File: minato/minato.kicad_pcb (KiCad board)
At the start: 2 copper layers, 400.1 x 144.5 mm, 220 parts, among them U2 STM32F103C8Tx

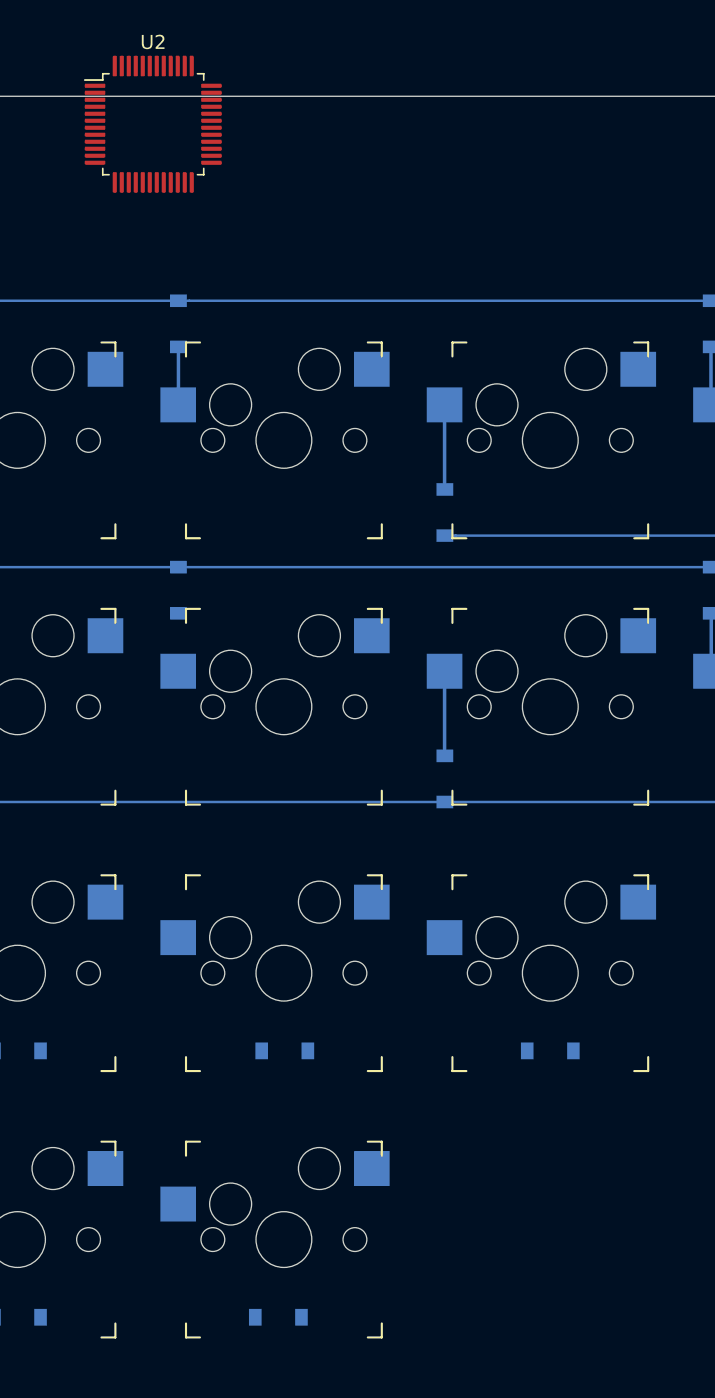
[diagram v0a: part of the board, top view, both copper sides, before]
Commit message: :sparkles: Add crystal + HW reset
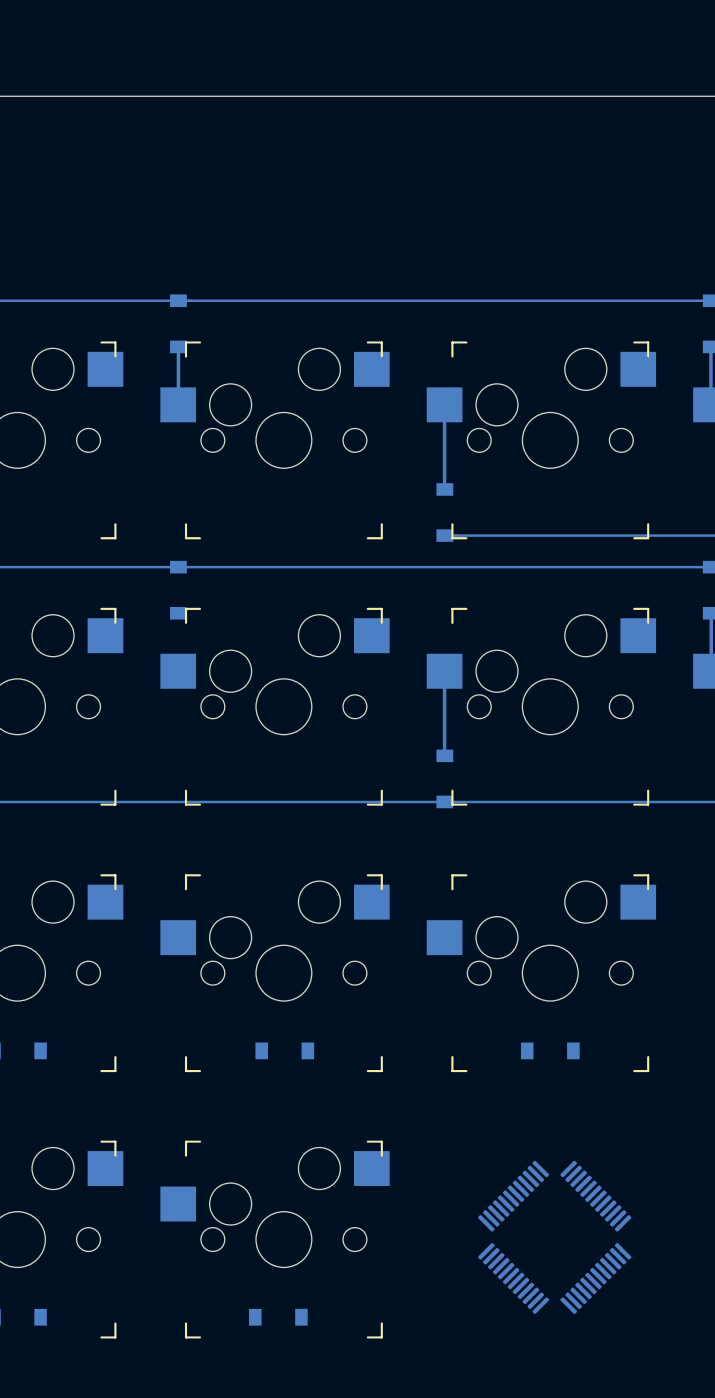
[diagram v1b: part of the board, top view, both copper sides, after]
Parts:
- U2: moved to B.Cu
- moved U2 84.6 mm to (94.0, 99.1), turned to 45 degrees

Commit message: :construction: WIP
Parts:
- removed the HOLE_M3 at (414.7, 20.2)
- removed the HOLE_M3 at (414.7, 159.1)
- removed the HOLE_M3 at (20.2, 159.1)
- added C1: 4.7nF, Capacitor_SMD:C_0805_2012Metric, F.Cu at (138.9, -7.29)
- added C10: 100nF, Capacitor_SMD:C_0805_2012Metric, F.Cu at (85.5, 95.2)
- added C11: 10nF, Capacitor_SMD:C_0805_2012Metric, F.Cu at (150.3, -22.3)
- added C12: 1uF, Capacitor_SMD:C_0805_2012Metric, F.Cu at (141.9, -12.3)
- added C2: 10uF, Capacitor_SMD:C_0805_2012Metric, F.Cu at (143.9, -27.4)
- added C3: 4.7nF, Capacitor_SMD:C_0805_2012Metric, F.Cu at (136.7, -23.8)
- added C6: 100nF, Capacitor_SMD:C_0805_2012Metric, F.Cu at (135.1, -16.1)
- added C7: 100nF, Capacitor_SMD:C_0805_2012Metric, F.Cu at (90.1, 107.2)
- added C8: 100nF, Capacitor_SMD:C_0805_2012Metric, F.Cu at (132.1, -7.15)
- added C9: 100nF, Capacitor_SMD:C_0805_2012Metric, F.Cu at (100.8, 104.4)
- added D106: 1N4148, keyboard_parts.pretty:D_SOD123W_hand, F.Cu at (137.1, -28.1)
- added D108: 1N4148, keyboard_parts.pretty:D_SOD123W_hand, F.Cu at (116.3, -18.3)
- added F1: Polyfuse_Small, Fuse:Fuse_1812_4532Metric, F.Cu at (125.2, -7.17)
- added HOLE_M3: VAL**, keyboard_parts.pretty:HOLE_M3, F.Cu at (414.3, 33.7)
- added HOLE_M3: VAL**, keyboard_parts.pretty:HOLE_M3, F.Cu at (414.3, 145.7)
- added HOLE_M3: VAL**, keyboard_parts.pretty:HOLE_M3, F.Cu at (20.6, 145.7)
- added J1: Conn_ARM_JTAG_SWD_10, Connector_IDC:IDC-Header_2x05_P2.54mm_Vertical, B.Cu at (89.3, 138.5)
- added J2: USB_C_Receptacle_USB2.0, Connector_USB:USB_C_Receptacle_GCT_USB4085, B.Cu at (46.8, 36.5)
- added Q1: DTC123J, Package_TO_SOT_SMD:SOT-23, F.Cu at (147.6, -17.6)
- added R1: 10k, keyboard_parts.pretty:R_2012, F.Cu at (151.9, -18.1)
- added R2: 1M, keyboard_parts.pretty:R_2012, F.Cu at (144.4, -8.06)
- added R3: 5.1k, keyboard_parts.pretty:R_2012, F.Cu at (151.9, -14.6)
- added R4: 5.1k, keyboard_parts.pretty:R_2012, F.Cu at (148.6, -9.00)
- added SW1: SW_Push, keyboard_parts.pretty:SW_ALPS_SKRP, F.Cu at (104.8, 99.2)
- added U1: MCP1700-3302E_SOT23, Package_TO_SOT_SMD:SOT-23, F.Cu at (147.6, -13.0)
- added Y1: 16MHz, local.pretty:OSC_CSTCE16M0V53-R0, F.Cu at (84.5, 102.8)
- D1, D10, D100, D101, D102, D103, D104, D105, D11, D12, D13, D14, D15, D16, D17, D18, D19, D2, D20, D21, D22, D23, D24, D25, D26, D27, D28, D29, D3, D30, D31, D32, D33, D34, D35, D36, D37, D38, D39, D4, D40, D41, D42, D43, D44, D45, D46, D47, D48, D49, D5, D50, D51, D52, D53, D54, D55, D56, D57, D58, D59, D6, D60, D61, D62, D63, D64, D65, D66, D67, D68, D69, D7, D70, D71, D72, D73, D74, D75, D76, D77, D78, D79, D8, D80, D81, D82, D83, D84, D85, D86, D87, D88, D89, D9, D90, D91, D92, D93, D94, D95, D96, D97, D98, D99: footprint Diode_SMD:D_SOD-123 -> keyboard_parts.pretty:D_SOD123W_hand
- U2: moved to F.Cu
- moved HOLE_M3 13.5 mm to (20.6, 33.7)
- moved U2 1.12 mm to (92.9, 99.2)
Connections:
- MX0:0 pad 1: Net-(MX0:0-Pad1) -> Col0
- U2 pad 1: Net-(U2-Pad1) -> VSS1
- U2 pad 23: Net-(U2-Pad23) -> VSS1
- U2 pad 24: Net-(U2-Pad24) -> 3.3V
- U2 pad 3: Net-(U2-Pad3) -> XTI
- U2 pad 35: Net-(U2-Pad35) -> VSS1
- U2 pad 36: Net-(U2-Pad36) -> 3.3V
- U2 pad 4: Net-(U2-Pad4) -> XTO
- U2 pad 44: Net-(U2-Pad44) -> BOOT0
- U2 pad 47: Net-(U2-Pad47) -> VSS1
- U2 pad 48: Net-(U2-Pad48) -> 3.3V
- U2 pad 8: Net-(U2-Pad8) -> VSS1
- U2 pad 9: Net-(U2-Pad9) -> 3.3V
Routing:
- net VSS1: track 0.00 -> 26.0 mm
- net 3.3V: track 0.00 -> 23.1 mm
- net XTO: track 0.00 -> 5.55 mm
- net XTI: track 0.00 -> 4.99 mm
- net Net-(D106-Pad2): track 0.00 -> 4.20 mm
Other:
- board size 400.1 x 144.5 mm -> 400.1 x 118.3 mm

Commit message: :construction: More PCB work
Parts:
- removed C10: 100nF, Capacitor_SMD:C_0805_2012Metric
- added Ce: 100nF, Capacitor_SMD:C_0805_2012Metric, F.Cu at (90.4, 91.9)
- moved C11 139.9 mm to (95.6, 106.4), turned to 180 degrees
- moved C12 129.6 mm to (95.6, 108.7), turned to 180 degrees
- moved D63 15.8 mm to (265.1, 47.6), turned to 180 degrees
- moved D64 15.8 mm to (265.1, 66.7), turned to 180 degrees
- moved D96 15.8 mm to (379.4, 47.6), turned to 180 degrees
- moved D1 15.8 mm to (36.5, 47.6), turned to 180 degrees
- moved D2 15.8 mm to (36.5, 66.7), turned to 180 degrees
- moved D22 15.8 mm to (112.7, 47.6), turned to 180 degrees
- moved D23 15.8 mm to (112.7, 66.7), turned to 180 degrees
- moved D31 15.8 mm to (150.8, 47.6), turned to 180 degrees
- moved D32 15.8 mm to (150.8, 66.7), turned to 180 degrees
- moved D43 15.8 mm to (188.9, 47.6), turned to 180 degrees
- moved D44 15.8 mm to (188.9, 66.7), turned to 180 degrees
- moved D12 15.8 mm to (74.6, 47.6), turned to 180 degrees
- moved D13 15.8 mm to (74.6, 66.7), turned to 180 degrees
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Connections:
- D1 pad 1: Row0 -> Net-(D1-Pad1)
- D1 pad 2: Net-(D1-Pad2) -> Col0
- D10 pad 1: Row7 -> Net-(D10-Pad1)
- D10 pad 2: Net-(D10-Pad2) -> Col0
- D100 pad 1: Row1 -> Net-(D100-Pad1)
- D100 pad 2: Net-(D100-Pad2) -> Col9
- D101 pad 1: Row2 -> Net-(D101-Pad1)
- D101 pad 2: Net-(D101-Pad2) -> Col9
- D102 pad 1: Row4 -> Net-(D102-Pad1)
- D102 pad 2: Net-(D102-Pad2) -> Col9
- D103 pad 1: Row6 -> Net-(D103-Pad1)
- D103 pad 2: Net-(D103-Pad2) -> Col8
- D104 pad 1: Row9 -> Net-(D104-Pad1)
- D104 pad 2: Net-(D104-Pad2) -> Col8
- D105 pad 1: Row11 -> Net-(D105-Pad1)
- D105 pad 2: Net-(D105-Pad2) -> Col5
- D11 pad 1: Row9 -> Net-(D11-Pad1)
- D11 pad 2: Net-(D11-Pad2) -> Col0
- D12 pad 1: Row0 -> Net-(D12-Pad1)
- D12 pad 2: Net-(D12-Pad2) -> Col1
- D13 pad 1: Row2 -> Net-(D13-Pad1)
- D13 pad 2: Net-(D13-Pad2) -> Col1
- D14 pad 1: Row4 -> Net-(D14-Pad1)
- D14 pad 2: Net-(D14-Pad2) -> Col1
- D15 pad 1: Row6 -> Net-(D15-Pad1)
- D15 pad 2: Net-(D15-Pad2) -> Col1
- D16 pad 1: Row8 -> Net-(D16-Pad1)
- D16 pad 2: Net-(D16-Pad2) -> Col1
- D17 pad 1: Row11 -> Net-(D17-Pad1)
- D17 pad 2: Net-(D17-Pad2) -> Col0
- D18 pad 1: Row1 -> Net-(D18-Pad1)
- D18 pad 2: Net-(D18-Pad2) -> Col1
- D19 pad 1: Row3 -> Net-(D19-Pad1)
- D19 pad 2: Net-(D19-Pad2) -> Col1
- D2 pad 1: Row2 -> Net-(D2-Pad1)
- D2 pad 2: Net-(D2-Pad2) -> Col0
- D20 pad 1: Row5 -> Net-(D20-Pad1)
- D20 pad 2: Net-(D20-Pad2) -> Col1
- D21 pad 1: Row9 -> Net-(D21-Pad1)
- D21 pad 2: Net-(D21-Pad2) -> Col1
- D22 pad 1: Row0 -> Net-(D22-Pad1)
- D22 pad 2: Net-(D22-Pad2) -> Col2
- D23 pad 1: Row2 -> Net-(D23-Pad1)
- D23 pad 2: Net-(D23-Pad2) -> Col2
- D24 pad 1: Row4 -> Net-(D24-Pad1)
- D24 pad 2: Net-(D24-Pad2) -> Col2
- D25 pad 1: Row7 -> Net-(D25-Pad1)
- D25 pad 2: Net-(D25-Pad2) -> Col1
- D26 pad 1: Row8 -> Net-(D26-Pad1)
- D26 pad 2: Net-(D26-Pad2) -> Col2
- D27 pad 1: Row10 -> Net-(D27-Pad1)
- D27 pad 2: Net-(D27-Pad2) -> Col1
- D28 pad 1: Row1 -> Net-(D28-Pad1)
- D28 pad 2: Net-(D28-Pad2) -> Col2
- D29 pad 1: Row3 -> Net-(D29-Pad1)
- D29 pad 2: Net-(D29-Pad2) -> Col2
- D3 pad 1: Row4 -> Net-(D3-Pad1)
- D3 pad 2: Net-(D3-Pad2) -> Col0
- D30 pad 1: Row11 -> Net-(D30-Pad1)
- D30 pad 2: Net-(D30-Pad2) -> Col1
- D31 pad 1: Row0 -> Net-(D31-Pad1)
- D31 pad 2: Net-(D31-Pad2) -> Col3
- D32 pad 1: Row2 -> Net-(D32-Pad1)
- D32 pad 2: Net-(D32-Pad2) -> Col3
- D33 pad 1: Row5 -> Net-(D33-Pad1)
- D33 pad 2: Net-(D33-Pad2) -> Col2
- D34 pad 1: Row6 -> Net-(D34-Pad1)
- D34 pad 2: Net-(D34-Pad2) -> Col2
- D35 pad 1: Row9 -> Net-(D35-Pad1)
- D35 pad 2: Net-(D35-Pad2) -> Col2
- D36 pad 1: Row10 -> Net-(D36-Pad1)
- D36 pad 2: Net-(D36-Pad2) -> Col2
- D37 pad 1: Row1 -> Net-(D37-Pad1)
- D37 pad 2: Net-(D37-Pad2) -> Col3
- D38 pad 1: Row3 -> Net-(D38-Pad1)
- D38 pad 2: Net-(D38-Pad2) -> Col3
- D39 pad 1: Row4 -> Net-(D39-Pad1)
- D39 pad 2: Net-(D39-Pad2) -> Col3
- D4 pad 1: Row6 -> Net-(D4-Pad1)
- D4 pad 2: Net-(D4-Pad2) -> Col0
- D40 pad 1: Row7 -> Net-(D40-Pad1)
- D40 pad 2: Net-(D40-Pad2) -> Col2
- D41 pad 1: Row8 -> Net-(D41-Pad1)
- D41 pad 2: Net-(D41-Pad2) -> Col3
- D42 pad 1: Row11 -> Net-(D42-Pad1)
- D42 pad 2: Net-(D42-Pad2) -> Col2
- D43 pad 1: Row0 -> Net-(D43-Pad1)
- D43 pad 2: Net-(D43-Pad2) -> Col4
- D44 pad 1: Row2 -> Net-(D44-Pad1)
- D44 pad 2: Net-(D44-Pad2) -> Col4
- D45 pad 1: Row5 -> Net-(D45-Pad1)
- D45 pad 2: Net-(D45-Pad2) -> Col3
- D46 pad 1: Row6 -> Net-(D46-Pad1)
- D46 pad 2: Net-(D46-Pad2) -> Col3
- D47 pad 1: Row9 -> Net-(D47-Pad1)
- D47 pad 2: Net-(D47-Pad2) -> Col3
- D48 pad 1: Row1 -> Net-(D48-Pad1)
- D48 pad 2: Net-(D48-Pad2) -> Col4
- D49 pad 1: Row3 -> Net-(D49-Pad1)
- D49 pad 2: Net-(D49-Pad2) -> Col4
- D5 pad 1: Row8 -> Net-(D5-Pad1)
- D5 pad 2: Net-(D5-Pad2) -> Col0
- D50 pad 1: Row4 -> Net-(D50-Pad1)
- D50 pad 2: Net-(D50-Pad2) -> Col4
- D51 pad 1: Row7 -> Net-(D51-Pad1)
- D51 pad 2: Net-(D51-Pad2) -> Col3
- D52 pad 1: Row8 -> Net-(D52-Pad1)
- D52 pad 2: Net-(D52-Pad2) -> Col4
- D53 pad 1: Row0 -> Net-(D53-Pad1)
- D53 pad 2: Net-(D53-Pad2) -> Col5
- D54 pad 1: Row2 -> Net-(D54-Pad1)
- D54 pad 2: Net-(D54-Pad2) -> Col5
- D55 pad 1: Row5 -> Net-(D55-Pad1)
- D55 pad 2: Net-(D55-Pad2) -> Col4
- D56 pad 1: Row6 -> Net-(D56-Pad1)
- D56 pad 2: Net-(D56-Pad2) -> Col4
- D57 pad 1: Row9 -> Net-(D57-Pad1)
- D57 pad 2: Net-(D57-Pad2) -> Col4
- D58 pad 1: Row1 -> Net-(D58-Pad1)
- D58 pad 2: Net-(D58-Pad2) -> Col5
- D59 pad 1: Row3 -> Net-(D59-Pad1)
- D59 pad 2: Net-(D59-Pad2) -> Col5
- D6 pad 1: Row10 -> Net-(D6-Pad1)
- D6 pad 2: Net-(D6-Pad2) -> Col0
- D60 pad 1: Row4 -> Net-(D60-Pad1)
- D60 pad 2: Net-(D60-Pad2) -> Col5
- D61 pad 1: Row7 -> Net-(D61-Pad1)
- D61 pad 2: Net-(D61-Pad2) -> Col4
- D62 pad 1: Row8 -> Net-(D62-Pad1)
- D62 pad 2: Net-(D62-Pad2) -> Col5
- D63 pad 1: Row0 -> Net-(D63-Pad1)
- D63 pad 2: Net-(D63-Pad2) -> Col6
- D64 pad 1: Row2 -> Net-(D64-Pad1)
- D64 pad 2: Net-(D64-Pad2) -> Col6
- D65 pad 1: Row5 -> Net-(D65-Pad1)
- D65 pad 2: Net-(D65-Pad2) -> Col5
- D66 pad 1: Row6 -> Net-(D66-Pad1)
- D66 pad 2: Net-(D66-Pad2) -> Col5
- D67 pad 1: Row9 -> Net-(D67-Pad1)
- D67 pad 2: Net-(D67-Pad2) -> Col5
- D68 pad 1: Row1 -> Net-(D68-Pad1)
- D68 pad 2: Net-(D68-Pad2) -> Col6
- D69 pad 1: Row3 -> Net-(D69-Pad1)
- D69 pad 2: Net-(D69-Pad2) -> Col6
- D7 pad 1: Row1 -> Net-(D7-Pad1)
- D7 pad 2: Net-(D7-Pad2) -> Col0
- D70 pad 1: Row4 -> Net-(D70-Pad1)
- D70 pad 2: Net-(D70-Pad2) -> Col6
- D71 pad 1: Row7 -> Net-(D71-Pad1)
- D71 pad 2: Net-(D71-Pad2) -> Col5
- D72 pad 1: Row8 -> Net-(D72-Pad1)
- D72 pad 2: Net-(D72-Pad2) -> Col6
- D73 pad 1: Row0 -> Net-(D73-Pad1)
- D73 pad 2: Net-(D73-Pad2) -> Col7
- D74 pad 1: Row2 -> Net-(D74-Pad1)
- D74 pad 2: Net-(D74-Pad2) -> Col7
- D75 pad 1: Row5 -> Net-(D75-Pad1)
- D75 pad 2: Net-(D75-Pad2) -> Col6
- D76 pad 1: Row6 -> Net-(D76-Pad1)
- D76 pad 2: Net-(D76-Pad2) -> Col6
- D77 pad 1: Row9 -> Net-(D77-Pad1)
- D77 pad 2: Net-(D77-Pad2) -> Col6
- D78 pad 1: Row10 -> Net-(D78-Pad1)
- D78 pad 2: Net-(D78-Pad2) -> Col3
- D79 pad 1: Row1 -> Net-(D79-Pad1)
- D79 pad 2: Net-(D79-Pad2) -> Col7
- D8 pad 1: Row3 -> Net-(D8-Pad1)
- D8 pad 2: Net-(D8-Pad2) -> Col0
- D80 pad 1: Row3 -> Net-(D80-Pad1)
- D80 pad 2: Net-(D80-Pad2) -> Col7
- D81 pad 1: Row4 -> Net-(D81-Pad1)
- D81 pad 2: Net-(D81-Pad2) -> Col7
- D82 pad 1: Row7 -> Net-(D82-Pad1)
- D82 pad 2: Net-(D82-Pad2) -> Col6
- D83 pad 1: Row8 -> Net-(D83-Pad1)
- D83 pad 2: Net-(D83-Pad2) -> Col7
- D84 pad 1: Row11 -> Net-(D84-Pad1)
- D84 pad 2: Net-(D84-Pad2) -> Col3
- D85 pad 1: Row0 -> Net-(D85-Pad1)
- D85 pad 2: Net-(D85-Pad2) -> Col8
- D86 pad 1: Row2 -> Net-(D86-Pad1)
- D86 pad 2: Net-(D86-Pad2) -> Col8
- D87 pad 1: Row5 -> Net-(D87-Pad1)
- D87 pad 2: Net-(D87-Pad2) -> Col7
- D88 pad 1: Row6 -> Net-(D88-Pad1)
- D88 pad 2: Net-(D88-Pad2) -> Col7
- D89 pad 1: Row9 -> Net-(D89-Pad1)
- D89 pad 2: Net-(D89-Pad2) -> Col7
- D9 pad 1: Row5 -> Net-(D9-Pad1)
- D9 pad 2: Net-(D9-Pad2) -> Col0
- D90 pad 1: Row10 -> Net-(D90-Pad1)
- D90 pad 2: Net-(D90-Pad2) -> Col4
- D91 pad 1: Row1 -> Net-(D91-Pad1)
- D91 pad 2: Net-(D91-Pad2) -> Col8
- D92 pad 1: Row3 -> Net-(D92-Pad1)
- D92 pad 2: Net-(D92-Pad2) -> Col8
- D93 pad 1: Row4 -> Net-(D93-Pad1)
- D93 pad 2: Net-(D93-Pad2) -> Col8
- D94 pad 1: Row7 -> Net-(D94-Pad1)
- D94 pad 2: Net-(D94-Pad2) -> Col7
- D95 pad 1: Row11 -> Net-(D95-Pad1)
- D95 pad 2: Net-(D95-Pad2) -> Col4
- D96 pad 1: Row0 -> Net-(D96-Pad1)
- D96 pad 2: Net-(D96-Pad2) -> Col9
- D97 pad 1: Row5 -> Net-(D97-Pad1)
- D97 pad 2: Net-(D97-Pad2) -> Col8
- D98 pad 1: Row8 -> Net-(D98-Pad1)
- D98 pad 2: Net-(D98-Pad2) -> Col8
- D99 pad 1: Row10 -> Net-(D99-Pad1)
- D99 pad 2: Net-(D99-Pad2) -> Col5
- MX0:0 pad 1: Col0 -> Net-(D1-Pad1)
- MX0:0 pad 2: Net-(D1-Pad2) -> Row0
- MX0:1 pad 1: Col0 -> Net-(D7-Pad1)
- MX0:1 pad 2: Net-(D7-Pad2) -> Row1
- MX0:10 pad 1: Col0 -> Net-(D6-Pad1)
- MX0:10 pad 2: Net-(D6-Pad2) -> Row10
- MX0:2 pad 1: Col0 -> Net-(D2-Pad1)
- MX0:2 pad 2: Net-(D2-Pad2) -> Row2
- MX0:3 pad 1: Col0 -> Net-(D8-Pad1)
- MX0:3 pad 2: Net-(D8-Pad2) -> Row3
- MX0:4 pad 1: Col0 -> Net-(D3-Pad1)
- MX0:4 pad 2: Net-(D3-Pad2) -> Row4
- MX0:5 pad 1: Col0 -> Net-(D9-Pad1)
- MX0:5 pad 2: Net-(D9-Pad2) -> Row5
- MX0:6 pad 1: Col0 -> Net-(D4-Pad1)
- MX0:6 pad 2: Net-(D4-Pad2) -> Row6
- MX0:7 pad 1: Col0 -> Net-(D10-Pad1)
- MX0:7 pad 2: Net-(D10-Pad2) -> Row7
- MX0:8 pad 1: Col0 -> Net-(D5-Pad1)
- MX0:8 pad 2: Net-(D5-Pad2) -> Row8
- MX0:9 pad 1: Col0 -> Net-(D11-Pad1)
- MX0:9 pad 2: Net-(D11-Pad2) -> Row9
- MX1:0 pad 1: Col1 -> Net-(D12-Pad1)
- MX1:0 pad 2: Net-(D12-Pad2) -> Row0
- MX1:1 pad 1: Col1 -> Net-(D18-Pad1)
- MX1:1 pad 2: Net-(D18-Pad2) -> Row1
- MX1:11 pad 1: Col1 -> Net-(D17-Pad1)
- MX1:11 pad 2: Net-(D17-Pad2) -> Row11
- MX1:2 pad 1: Col1 -> Net-(D13-Pad1)
- MX1:2 pad 2: Net-(D13-Pad2) -> Row2
- MX1:3 pad 1: Col1 -> Net-(D19-Pad1)
- MX1:3 pad 2: Net-(D19-Pad2) -> Row3
- MX1:4 pad 1: Col1 -> Net-(D14-Pad1)
- MX1:4 pad 2: Net-(D14-Pad2) -> Row4
- MX1:5 pad 1: Col1 -> Net-(D20-Pad1)
- MX1:5 pad 2: Net-(D20-Pad2) -> Row5
- MX1:6 pad 1: Col1 -> Net-(D15-Pad1)
- MX1:6 pad 2: Net-(D15-Pad2) -> Row6
- MX1:8 pad 1: Col1 -> Net-(D16-Pad1)
- MX1:8 pad 2: Net-(D16-Pad2) -> Row8
- MX1:9 pad 1: Col1 -> Net-(D21-Pad1)
- MX1:9 pad 2: Net-(D21-Pad2) -> Row9
- MX2:0 pad 1: Col2 -> Net-(D22-Pad1)
- MX2:0 pad 2: Net-(D22-Pad2) -> Row0
- MX2:1 pad 1: Col2 -> Net-(D28-Pad1)
- MX2:1 pad 2: Net-(D28-Pad2) -> Row1
- MX2:10 pad 1: Col2 -> Net-(D27-Pad1)
- MX2:10 pad 2: Net-(D27-Pad2) -> Row10
- MX2:11 pad 1: Col2 -> Net-(D30-Pad1)
- MX2:11 pad 2: Net-(D30-Pad2) -> Row11
- MX2:2 pad 1: Col2 -> Net-(D23-Pad1)
- MX2:2 pad 2: Net-(D23-Pad2) -> Row2
- MX2:3 pad 1: Col2 -> Net-(D29-Pad1)
- MX2:3 pad 2: Net-(D29-Pad2) -> Row3
- MX2:4 pad 1: Col2 -> Net-(D24-Pad1)
- MX2:4 pad 2: Net-(D24-Pad2) -> Row4
- MX2:6 pad 1: Col2 -> Net-(D25-Pad1)
- MX2:6 pad 2: Net-(D25-Pad2) -> Row7
- MX2:8 pad 1: Col2 -> Net-(D26-Pad1)
- MX2:8 pad 2: Net-(D26-Pad2) -> Row8
- MX3:0 pad 1: Col3 -> Net-(D31-Pad1)
- MX3:0 pad 2: Net-(D31-Pad2) -> Row0
- MX3:1 pad 1: Col3 -> Net-(D37-Pad1)
- MX3:1 pad 2: Net-(D37-Pad2) -> Row1
- MX3:10 pad 1: Col3 -> Net-(D36-Pad1)
- MX3:10 pad 2: Net-(D36-Pad2) -> Row10
- MX3:11 pad 1: Col3 -> Net-(D42-Pad1)
- MX3:11 pad 2: Net-(D42-Pad2) -> Row11
- MX3:2 pad 1: Col3 -> Net-(D32-Pad1)
- MX3:2 pad 2: Net-(D32-Pad2) -> Row2
- MX3:3 pad 1: Col3 -> Net-(D38-Pad1)
- MX3:3 pad 2: Net-(D38-Pad2) -> Row3
- MX3:4 pad 1: Col3 -> Net-(D39-Pad1)
- MX3:4 pad 2: Net-(D39-Pad2) -> Row4
- MX3:5 pad 1: Col3 -> Net-(D33-Pad1)
- MX3:5 pad 2: Net-(D33-Pad2) -> Row5
- MX3:6 pad 1: Col3 -> Net-(D34-Pad1)
- MX3:6 pad 2: Net-(D34-Pad2) -> Row6
- MX3:7 pad 1: Col3 -> Net-(D40-Pad1)
- MX3:7 pad 2: Net-(D40-Pad2) -> Row7
- MX3:8 pad 1: Col3 -> Net-(D41-Pad1)
- MX3:8 pad 2: Net-(D41-Pad2) -> Row8
- MX3:9 pad 1: Col3 -> Net-(D35-Pad1)
- MX3:9 pad 2: Net-(D35-Pad2) -> Row9
- MX4:0 pad 1: Col4 -> Net-(D43-Pad1)
- MX4:0 pad 2: Net-(D43-Pad2) -> Row0
- MX4:1 pad 1: Col4 -> Net-(D48-Pad1)
- MX4:1 pad 2: Net-(D48-Pad2) -> Row1
- MX4:2 pad 1: Col4 -> Net-(D44-Pad1)
- MX4:2 pad 2: Net-(D44-Pad2) -> Row2
- MX4:3 pad 1: Col4 -> Net-(D49-Pad1)
- MX4:3 pad 2: Net-(D49-Pad2) -> Row3
- MX4:4 pad 1: Col4 -> Net-(D50-Pad1)
- MX4:4 pad 2: Net-(D50-Pad2) -> Row4
- MX4:5 pad 1: Col4 -> Net-(D45-Pad1)
- MX4:5 pad 2: Net-(D45-Pad2) -> Row5
- MX4:6 pad 1: Col4 -> Net-(D46-Pad1)
- MX4:6 pad 2: Net-(D46-Pad2) -> Row6
- MX4:7 pad 1: Col4 -> Net-(D51-Pad1)
- MX4:7 pad 2: Net-(D51-Pad2) -> Row7
- MX4:8 pad 1: Col4 -> Net-(D52-Pad1)
- MX4:8 pad 2: Net-(D52-Pad2) -> Row8
- MX4:9 pad 1: Col4 -> Net-(D47-Pad1)
- MX4:9 pad 2: Net-(D47-Pad2) -> Row9
- MX5:0 pad 1: Col5 -> Net-(D53-Pad1)
- MX5:0 pad 2: Net-(D53-Pad2) -> Row0
- MX5:1 pad 1: Col5 -> Net-(D58-Pad1)
- MX5:1 pad 2: Net-(D58-Pad2) -> Row1
- MX5:2 pad 1: Col5 -> Net-(D54-Pad1)
- MX5:2 pad 2: Net-(D54-Pad2) -> Row2
- MX5:3 pad 1: Col5 -> Net-(D59-Pad1)
- MX5:3 pad 2: Net-(D59-Pad2) -> Row3
- MX5:4 pad 1: Col5 -> Net-(D60-Pad1)
- MX5:4 pad 2: Net-(D60-Pad2) -> Row4
- MX5:5 pad 1: Col5 -> Net-(D55-Pad1)
- MX5:5 pad 2: Net-(D55-Pad2) -> Row5
- MX5:6 pad 1: Col5 -> Net-(D56-Pad1)
- MX5:6 pad 2: Net-(D56-Pad2) -> Row6
- MX5:7 pad 1: Col5 -> Net-(D61-Pad1)
- MX5:7 pad 2: Net-(D61-Pad2) -> Row7
- MX5:8 pad 1: Col5 -> Net-(D62-Pad1)
- MX5:8 pad 2: Net-(D62-Pad2) -> Row8
- MX5:9 pad 1: Col5 -> Net-(D57-Pad1)
- MX5:9 pad 2: Net-(D57-Pad2) -> Row9
- MX6:0 pad 1: Col6 -> Net-(D63-Pad1)
- MX6:0 pad 2: Net-(D63-Pad2) -> Row0
- MX6:1 pad 1: Col6 -> Net-(D68-Pad1)
- MX6:1 pad 2: Net-(D68-Pad2) -> Row1
- MX6:2 pad 1: Col6 -> Net-(D64-Pad1)
- MX6:2 pad 2: Net-(D64-Pad2) -> Row2
- MX6:3 pad 1: Col6 -> Net-(D69-Pad1)
- MX6:3 pad 2: Net-(D69-Pad2) -> Row3
- MX6:4 pad 1: Col6 -> Net-(D70-Pad1)
- MX6:4 pad 2: Net-(D70-Pad2) -> Row4
- MX6:5 pad 1: Col6 -> Net-(D65-Pad1)
- MX6:5 pad 2: Net-(D65-Pad2) -> Row5
- MX6:6 pad 1: Col6 -> Net-(D66-Pad1)
- MX6:6 pad 2: Net-(D66-Pad2) -> Row6
- MX6:7 pad 1: Col6 -> Net-(D71-Pad1)
- MX6:7 pad 2: Net-(D71-Pad2) -> Row7
- MX6:8 pad 1: Col6 -> Net-(D72-Pad1)
- MX6:8 pad 2: Net-(D72-Pad2) -> Row8
- MX6:9 pad 1: Col6 -> Net-(D67-Pad1)
- MX6:9 pad 2: Net-(D67-Pad2) -> Row9
- MX7:0 pad 1: Col7 -> Net-(D73-Pad1)
- MX7:0 pad 2: Net-(D73-Pad2) -> Row0
- MX7:1 pad 1: Col7 -> Net-(D79-Pad1)
- MX7:1 pad 2: Net-(D79-Pad2) -> Row1
- MX7:10 pad 1: Col7 -> Net-(D78-Pad1)
- MX7:10 pad 2: Net-(D78-Pad2) -> Row10
- MX7:11 pad 1: Col7 -> Net-(D84-Pad1)
- MX7:11 pad 2: Net-(D84-Pad2) -> Row11
- MX7:2 pad 1: Col7 -> Net-(D74-Pad1)
- MX7:2 pad 2: Net-(D74-Pad2) -> Row2
- MX7:3 pad 1: Col7 -> Net-(D80-Pad1)
- MX7:3 pad 2: Net-(D80-Pad2) -> Row3
- MX7:4 pad 1: Col7 -> Net-(D81-Pad1)
- MX7:4 pad 2: Net-(D81-Pad2) -> Row4
- MX7:5 pad 1: Col7 -> Net-(D75-Pad1)
- MX7:5 pad 2: Net-(D75-Pad2) -> Row5
- MX7:6 pad 1: Col7 -> Net-(D76-Pad1)
- MX7:6 pad 2: Net-(D76-Pad2) -> Row6
- MX7:7 pad 1: Col7 -> Net-(D82-Pad1)
- MX7:7 pad 2: Net-(D82-Pad2) -> Row7
- MX7:8 pad 1: Col7 -> Net-(D83-Pad1)
- MX7:8 pad 2: Net-(D83-Pad2) -> Row8
- MX7:9 pad 1: Col7 -> Net-(D77-Pad1)
- MX7:9 pad 2: Net-(D77-Pad2) -> Row9
- MX8:0 pad 1: Col8 -> Net-(D85-Pad1)
- MX8:0 pad 2: Net-(D85-Pad2) -> Row0
- MX8:1 pad 1: Col8 -> Net-(D91-Pad1)
- MX8:1 pad 2: Net-(D91-Pad2) -> Row1
- MX8:10 pad 1: Col8 -> Net-(D90-Pad1)
- MX8:10 pad 2: Net-(D90-Pad2) -> Row10
- MX8:11 pad 1: Col8 -> Net-(D95-Pad1)
- MX8:11 pad 2: Net-(D95-Pad2) -> Row11
- MX8:2 pad 1: Col8 -> Net-(D86-Pad1)
- MX8:2 pad 2: Net-(D86-Pad2) -> Row2
- MX8:3 pad 1: Col8 -> Net-(D92-Pad1)
- MX8:3 pad 2: Net-(D92-Pad2) -> Row3
- MX8:4 pad 1: Col8 -> Net-(D93-Pad1)
- MX8:4 pad 2: Net-(D93-Pad2) -> Row4
- MX8:5 pad 1: Col8 -> Net-(D87-Pad1)
- MX8:5 pad 2: Net-(D87-Pad2) -> Row5
- MX8:6 pad 1: Col8 -> Net-(D88-Pad1)
- MX8:6 pad 2: Net-(D88-Pad2) -> Row6
- MX8:7 pad 1: Col8 -> Net-(D94-Pad1)
- MX8:7 pad 2: Net-(D94-Pad2) -> Row7
- MX8:9 pad 1: Col8 -> Net-(D89-Pad1)
- MX8:9 pad 2: Net-(D89-Pad2) -> Row9
- MX9:0 pad 1: Col9 -> Net-(D96-Pad1)
- MX9:0 pad 2: Net-(D96-Pad2) -> Row0
- MX9:1 pad 1: Col9 -> Net-(D100-Pad1)
- MX9:1 pad 2: Net-(D100-Pad2) -> Row1
- MX9:10 pad 1: Col9 -> Net-(D99-Pad1)
- MX9:10 pad 2: Net-(D99-Pad2) -> Row10
- MX9:11 pad 1: Col9 -> Net-(D105-Pad1)
- MX9:11 pad 2: Net-(D105-Pad2) -> Row11
- MX9:2 pad 1: Col9 -> Net-(D101-Pad1)
- MX9:2 pad 2: Net-(D101-Pad2) -> Row2
- MX9:4 pad 1: Col9 -> Net-(D102-Pad1)
- MX9:4 pad 2: Net-(D102-Pad2) -> Row4
- MX9:5 pad 1: Col9 -> Net-(D97-Pad1)
- MX9:5 pad 2: Net-(D97-Pad2) -> Row5
- MX9:6 pad 1: Col9 -> Net-(D103-Pad1)
- MX9:6 pad 2: Net-(D103-Pad2) -> Row6
- MX9:8 pad 1: Col9 -> Net-(D98-Pad1)
- MX9:8 pad 2: Net-(D98-Pad2) -> Row8
- MX9:9 pad 1: Col9 -> Net-(D104-Pad1)
- MX9:9 pad 2: Net-(D104-Pad2) -> Row9
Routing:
- net Row2: track 361.9 -> 0.00 mm
- net Row0: track 342.9 -> 0.00 mm
- net Row3: track 315.3 -> 0.00 mm
- net Row1: track 304.8 -> 0.00 mm
- net Col9: track 201.1 -> 0.00 mm, vias 10 -> 0
- net VSS1: track 26.0 -> 47.7 mm
- net Net-(D79-Pad2): track 6.06 -> 0.00 mm
- net Net-(D100-Pad2): track 6.06 -> 0.00 mm
- net Net-(D8-Pad2): track 6.06 -> 0.00 mm
- net Net-(D58-Pad2): track 6.06 -> 0.00 mm
- net Net-(D48-Pad2): track 6.06 -> 0.00 mm
- net Net-(D37-Pad2): track 6.06 -> 0.00 mm
- net Net-(D28-Pad2): track 6.06 -> 0.00 mm
- net Net-(D19-Pad2): track 6.06 -> 0.00 mm
- net Net-(D18-Pad2): track 6.06 -> 0.00 mm
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
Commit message: :sparkles: Place components on PCB
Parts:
- moved Q1 143.2 mm to (80.0, 108.7), turned to 270 degrees
- moved D106 136.3 mm to (81.8, 96.5), turned to 180 degrees
- moved C2 131.9 mm to (82.6, 89.4)
- moved C1 131.6 mm to (76.7, 108.7), turned to 270 degrees
- moved R1 130.7 mm to (82.6, 92.7), turned to 180 degrees
- moved U1 122.1 mm to (44.7, 52.8), turned to 90 degrees
- moved R3 121.3 mm to (40.1, 32.5), turned to 90 degrees
- moved C6 119.2 mm to (44.7, 61.5), turned to 270 degrees
- moved R4 113.3 mm to (43.2, 32.5), turned to 90 degrees
- moved C8 108.3 mm to (48.3, 61.5), turned to 270 degrees
- moved C3 103.9 mm to (49.3, 32.3), turned to 270 degrees
- moved D108 102.4 mm to (46.5, 56.6)
- moved R2 100.5 mm to (52.3, 32.3), turned to 270 degrees
- moved F1 97.0 mm to (44.7, 47.0), turned to 90 degrees
- moved SW1 26.9 mm to (80.0, 103.6), turned to 270 degrees
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- renumbered Ce to C10
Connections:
- U2 pad 32: D- -> DBUS-
- U2 pad 33: D+ -> DBUS+
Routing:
- net DBUS-: track 0.00 -> 102.1 mm
- net DBUS+: track 0.00 -> 100.0 mm
- net 3.3V: track 17.8 -> 103.1 mm
- net VSS1: track 47.7 -> 128.4 mm, vias 0 -> 1
- net Row0: track 0.00 -> 46.9 mm
- net NRST: track 0.00 -> 21.9 mm, vias 0 -> 2
- net VBUS: track 0.00 -> 18.2 mm
- net Net-(J2-PadA5): track 0.00 -> 18.1 mm, vias 0 -> 1
- net Net-(C3-Pad1): track 0.00 -> 16.2 mm
- net Net-(D106-Pad2): track 0.00 -> 15.7 mm
- net BOOT0: track 0.00 -> 14.6 mm
- net Net-(D15-Pad1): track 0.00 -> 13.2 mm
- net Net-(D16-Pad1): track 0.00 -> 13.0 mm
- net 5V: track 0.00 -> 11.5 mm
- net Net-(J2-PadB5): track 0.00 -> 11.3 mm, vias 0 -> 1
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
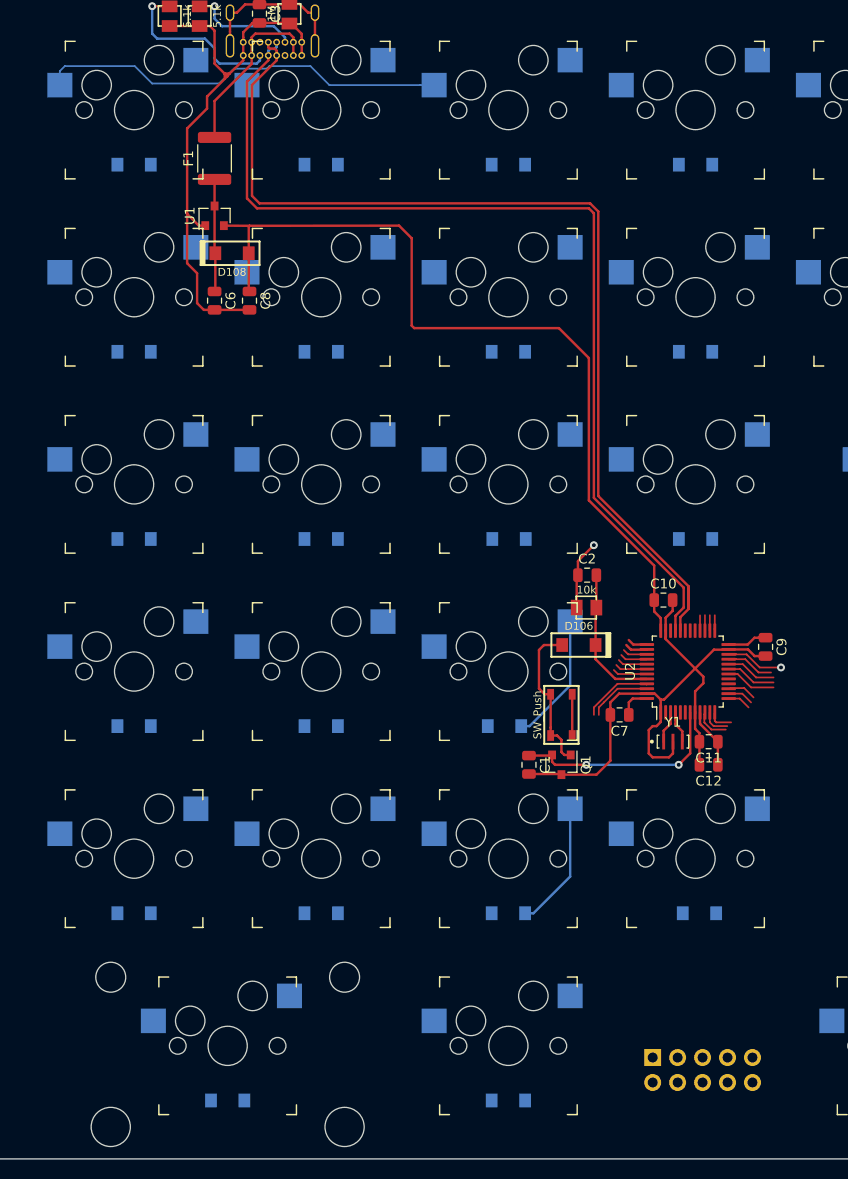
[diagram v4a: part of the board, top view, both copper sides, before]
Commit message: :sparkles: Wire up USB-C receptacle
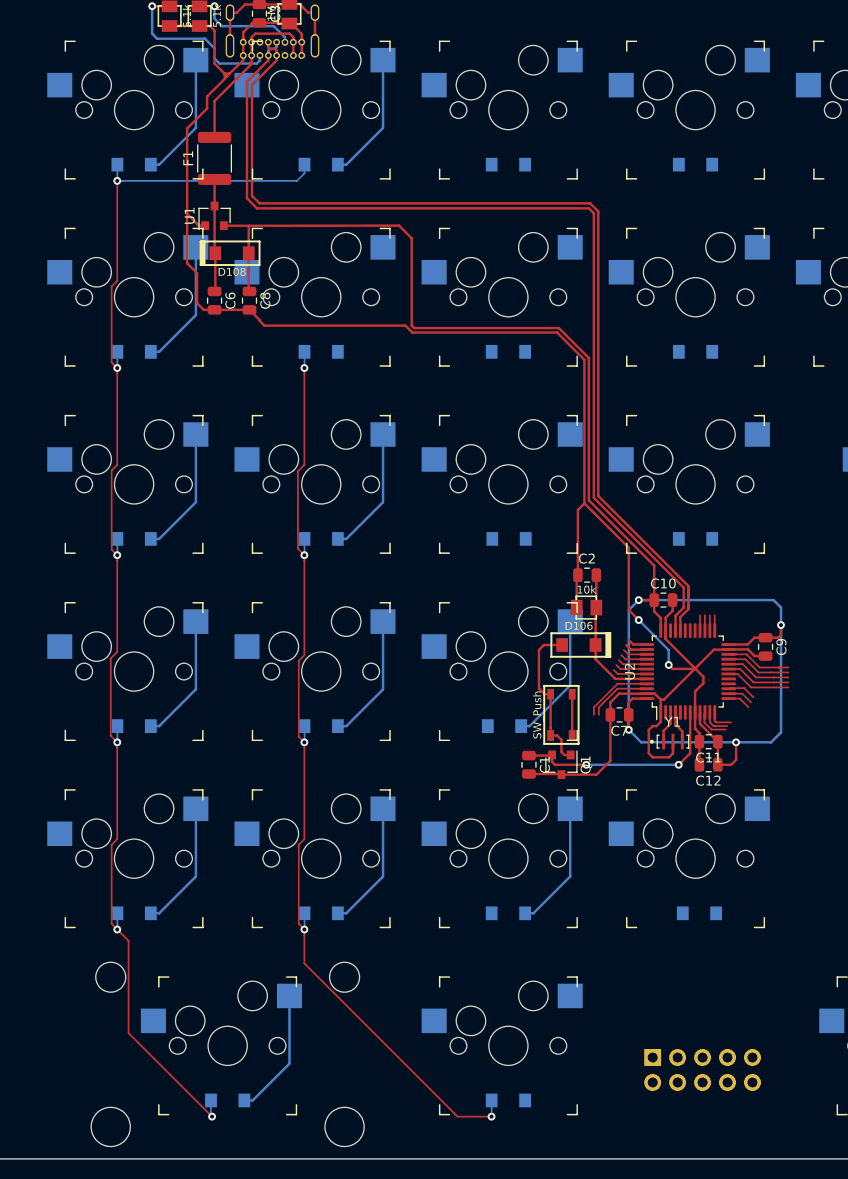
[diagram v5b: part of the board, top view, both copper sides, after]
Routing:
- net Col0: track 5.14 -> 234.0 mm, vias 0 -> 11
- net VSS1: track 128.4 -> 206.0 mm, vias 1 -> 2
- net 3.3V: track 103.1 -> 170.3 mm, vias 0 -> 4
- net Row0: track 46.9 -> 6.65 mm
- net Net-(D5-Pad1): track 0.00 -> 13.0 mm
- net Net-(D4-Pad1): track 0.00 -> 13.0 mm
- net Net-(D2-Pad1): track 0.00 -> 13.0 mm
- net Net-(D11-Pad1): track 0.00 -> 13.0 mm
- net Net-(D10-Pad1): track 0.00 -> 13.0 mm
- net Net-(D1-Pad1): track 0.00 -> 13.0 mm
- net Net-(D3-Pad1): track 0.00 -> 13.0 mm
- net Net-(D7-Pad1): track 0.00 -> 13.0 mm
- net Net-(D6-Pad1): track 0.00 -> 13.0 mm
- net Net-(D9-Pad1): track 0.00 -> 13.0 mm
- net Col2: track 5.13 -> 6.65 mm
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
